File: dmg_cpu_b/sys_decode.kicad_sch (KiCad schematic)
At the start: 82 parts, among them T1 IBUF, T2 IBUF

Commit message: CH1 Regs page completed.
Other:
- company: (none) -> CC-BY-SA-4.0 Régis Galland & Michael Singer -- Derived work from Furrtek
- title: (none) -> DMG CPU B
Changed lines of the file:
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@@
 (kicad_sch (version 20211123) (generator eeschema)
   (paper "A3")
+  (title_block
+    (title "DMG CPU B")
+    (date "2022-03-12")
+    (rev "0")
+    (company "CC-BY-SA-4.0 Régis Galland & Michael Singer -- Derived work from Furrtek")
+    (comment 1 "https://github.com/msinger/dmg-schematics")
+  )
   (junction (at 48.895 224.79) (diameter 0) (color 0 0 0 0)
   )

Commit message: First lot of fixes based on issues found.
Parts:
- added ADYR, AFOP: INVERTER_B, symbol DMG_CPU_Cells:INVERTER_B
- added AJEC, AKAJ, ANOC, ARAR, ASUZ, ATAJ, BEDA, BENU: TRI_INV_IF0, symbol DMG_CPU_Cells:TRI_INV_IF0
- added APYS: NOR_2, symbol DMG_CPU_Cells:NOR_2
- added AXYN: INVERTER_A, symbol DMG_CPU_Cells:INVERTER_A
- renumbered RESET to ~{RESET}
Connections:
- net BEDO: now also AXYN.1
- net D0: now also ANOC.3
- net D1: now also ATAJ.3
- net D2: now also AJEC.3
- net D3: now also ASUZ.3
- net D4: now also BENU.3
- net D5: now also AKAJ.3
- net D6: now also ARAR.3
- net D7: now also BEDA.3
- net GND: now also AJEC.2, AKAJ.2, ANOC.2, ARAR.2, ASUZ.2, ATAJ.2, BEDA.2, BENU.2
- net T1~{T2}: now also APYS.1
- new net: AFOP.2, AJEC.1 (~{ENA}), AKAJ.1 (~{ENA}), ANOC.1 (~{ENA}), ARAR.1 (~{ENA}), ASUZ.1 (~{ENA}), ATAJ.1 (~{ENA}), BEDA.1 (~{ENA}), BENU.1 (~{ENA})
- new net: ADYR.2, APYS.2
- new net: AFOP.1, APYS.3
- new net: ADYR.1, AXYN.2
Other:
- note removed: "This part is activated in test mode."
- moved on the sheet: AMUT, APER, APET, BAKO, BURO, LECO, LEXY, RARU, RASE, REJY, REKA, ROMY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

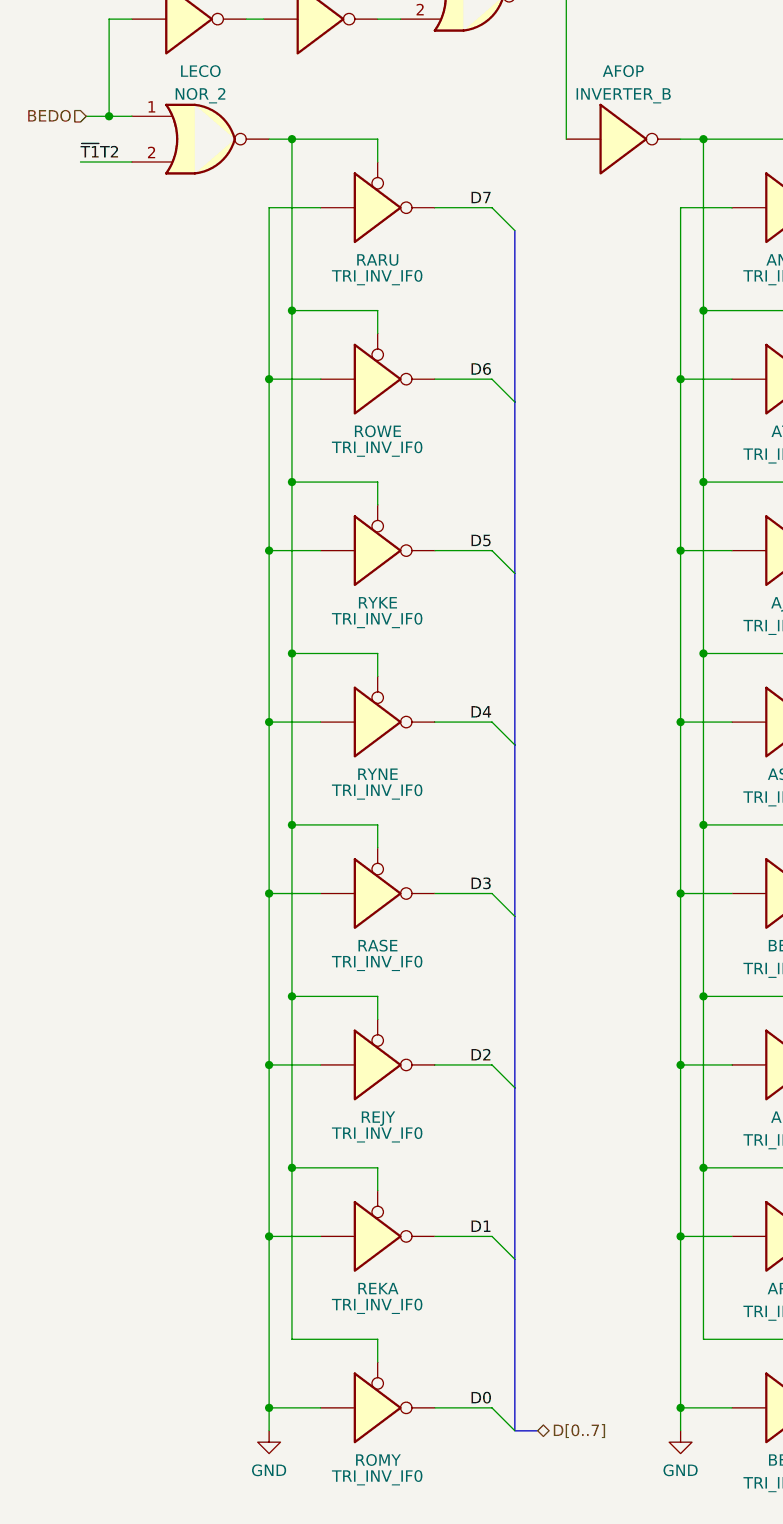
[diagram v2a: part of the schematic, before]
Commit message: CH1 SWEEP page added.
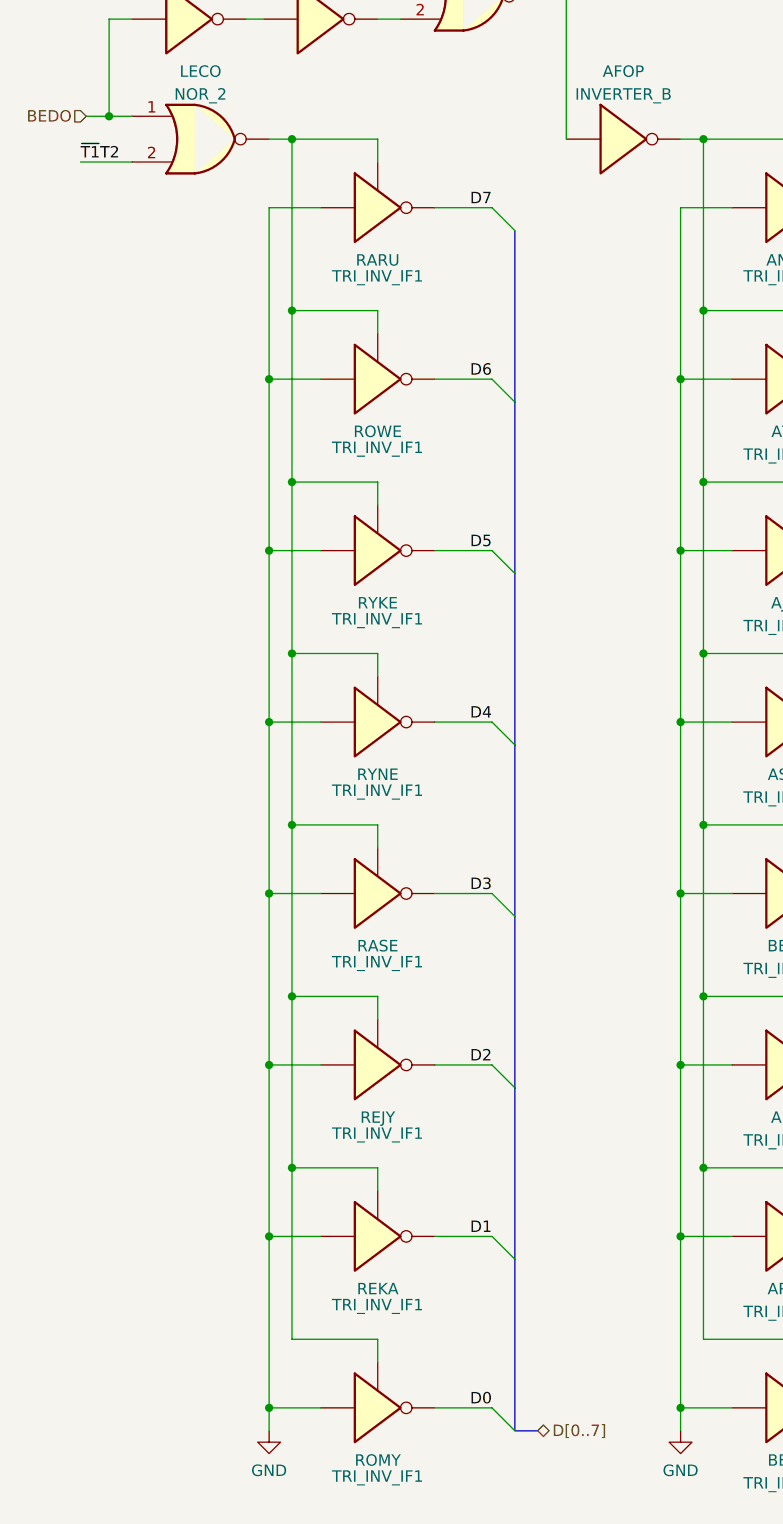
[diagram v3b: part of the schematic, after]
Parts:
- RARU, RASE, REJY, REKA, ROMY, ROWE, RYKE, RYNE: value TRI_INV_IF0 -> TRI_INV_IF1; symbol DMG_CPU_Cells:TRI_INV_IF0 -> DMG_CPU_Cells:TRI_INV_IF1
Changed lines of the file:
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@@
     (pin "2")
   )
-  (symbol (lib_name "TRI_INV_IF0_7") (lib_id "DMG_CPU_Cells:TRI_INV_IF0") (at 56.515 247.65 0) (unit 1)
+  (symbol (lib_id "DMG_CPU_Cells:TRI_INV_IF1") (at 56.515 247.65 0) (unit 1)
     (in_bom yes) (on_board yes) (fields_autoplaced)
     (property "Reference" "REKA" (id 0) (at 56.515 253.4904 0))
-    (property "Value" "TRI_INV_IF0" (id 1) (at 56.515 255.27 0))
+    (property "Value" "TRI_INV_IF1" (id 1) (at 56.515 255.27 0))
     (property "Footprint" "" (id 2) (at 53.975 247.65 0)
       (effects (font (size 1.27 1.27)) hide)
     )
-    (property "Datasheet" "http://iceboy.a-singer.de/doc/dmg_cells.html#tri_inv_if0" (id 3) (at 57.785 257.81 0)
+    (property "Datasheet" "http://iceboy.a-singer.de/doc/dmg_cells.html#tri_inv_if1" (id 3) (at 57.785 257.81 0)
       (effects (font (size 1.27 1.27)) hide)
     )
@@
     (pin "2")
   )
-  (symbol (lib_name "TRI_INV_IF0_3") (lib_id "DMG_CPU_Cells:TRI_INV_IF0") (at 56.515 171.45 0) (unit 1)
+  (symbol (lib_id "DMG_CPU_Cells:TRI_INV_IF1") (at 56.515 171.45 0) (unit 1)
     (in_bom yes) (on_board yes) (fields_autoplaced)
     (property "Reference" "RYKE" (id 0) (at 56.515 177.2904 0))
-    (property "Value" "TRI_INV_IF0" (id 1) (at 56.515 179.07 0))
+    (property "Value" "TRI_INV_IF1" (id 1) (at 56.515 179.07 0))
     (property "Footprint" "" (id 2) (at 53.975 171.45 0)
       (effects (font (size 1.27 1.27)) hide)
     )
-    (property "Datasheet" "http://iceboy.a-singer.de/doc/dmg_cells.html#tri_inv_if0" (id 3) (at 57.785 181.61 0)
-      (effects (font (size 1.27 1.27)) hide)
-    )
-    (pin "2")
-    (pin "3")
-    (pin "1")
-  )
-  (symbol (lib_name "TRI_INV_IF0_5") (lib_id "DMG_CPU_Cells:TRI_INV_IF0") (at 56.515 266.7 0) (unit 1)
+    (property "Datasheet" "http://iceboy.a-singer.de/doc/dmg_cells.html#tri_inv_if1" (id 3) (at 57.785 181.61 0)
+      (effects (font (size 1.27 1.27)) hide)
+    )
+    (pin "2")
+    (pin "3")
+    (pin "1")
+  )
+  (symbol (lib_id "DMG_CPU_Cells:TRI_INV_IF1") (at 56.515 266.7 0) (unit 1)
     (in_bom yes) (on_board yes) (fields_autoplaced)
     (property "Reference" "ROMY" (id 0) (at 56.515 272.5404 0))
-    (property "Value" "TRI_INV_IF0" (id 1) (at 56.515 274.32 0))
+    (property "Value" "TRI_INV_IF1" (id 1) (at 56.515 274.32 0))
     (property "Footprint" "" (id 2) (at 53.975 266.7 0)
       (effects (font (size 1.27 1.27)) hide)
     )
-    (property "Datasheet" "http://iceboy.a-singer.de/doc/dmg_cells.html#tri_inv_if0" (id 3) (at 57.785 276.86 0)
+    (property "Datasheet" "http://iceboy.a-singer.de/doc/dmg_cells.html#tri_inv_if1" (id 3) (at 57.785 276.86 0)
       (effects (font (size 1.27 1.27)) hide)
     )
@@
     (pin "2")
   )
-  (symbol (lib_name "TRI_INV_IF0_6") (lib_id "DMG_CPU_Cells:TRI_INV_IF0") (at 56.515 228.6 0) (unit 1)
+  (symbol (lib_id "DMG_CPU_Cells:TRI_INV_IF1") (at 56.515 228.6 0) (unit 1)
     (in_bom yes) (on_board yes) (fields_autoplaced)
     (property "Reference" "REJY" (id 0) (at 56.515 234.4404 0))
-    (property "Value" "TRI_INV_IF0" (id 1) (at 56.515 236.22 0))
+    (property "Value" "TRI_INV_IF1" (id 1) (at 56.515 236.22 0))
     (property "Footprint" "" (id 2) (at 53.975 228.6 0)
       (effects (font (size 1.27 1.27)) hide)
     )
-    (property "Datasheet" "http://iceboy.a-singer.de/doc/dmg_cells.html#tri_inv_if0" (id 3) (at 57.785 238.76 0)
-      (effects (font (size 1.27 1.27)) hide)
-    )
-    (pin "2")
-    (pin "3")
-    (pin "1")
-  )
-  (symbol (lib_name "TRI_INV_IF0_4") (lib_id "DMG_CPU_Cells:TRI_INV_IF0") (at 56.515 190.5 0) (unit 1)
+    (property "Datasheet" "http://iceboy.a-singer.de/doc/dmg_cells.html#tri_inv_if1" (id 3) (at 57.785 238.76 0)
+      (effects (font (size 1.27 1.27)) hide)
+    )
+    (pin "2")
+    (pin "3")
+    (pin "1")
+  )
+  (symbol (lib_id "DMG_CPU_Cells:TRI_INV_IF1") (at 56.515 190.5 0) (unit 1)
     (in_bom yes) (on_board yes) (fields_autoplaced)
     (property "Reference" "RYNE" (id 0) (at 56.515 196.3404 0))
-    (property "Value" "TRI_INV_IF0" (id 1) (at 56.515 198.12 0))
+    (property "Value" "TRI_INV_IF1" (id 1) (at 56.515 198.12 0))
     (property "Footprint" "" (id 2) (at 53.975 190.5 0)
       (effects (font (size 1.27 1.27)) hide)
     )
-    (property "Datasheet" "http://iceboy.a-singer.de/doc/dmg_cells.html#tri_inv_if0" (id 3) (at 57.785 200.66 0)
+    (property "Datasheet" "http://iceboy.a-singer.de/doc/dmg_cells.html#tri_inv_if1" (id 3) (at 57.785 200.66 0)
       (effects (font (size 1.27 1.27)) hide)
     )
@@
     (pin "3")
   )
-  (symbol (lib_name "TRI_INV_IF0_1") (lib_id "DMG_CPU_Cells:TRI_INV_IF0") (at 56.515 152.4 0) (unit 1)
+  (symbol (lib_id "DMG_CPU_Cells:TRI_INV_IF1") (at 56.515 152.4 0) (unit 1)
     (in_bom yes) (on_board yes) (fields_autoplaced)
     (property "Reference" "ROWE" (id 0) (at 56.515 158.2404 0))
-    (property "Value" "TRI_INV_IF0" (id 1) (at 56.515 160.02 0))
+    (property "Value" "TRI_INV_IF1" (id 1) (at 56.515 160.02 0))
     (property "Footprint" "" (id 2) (at 53.975 152.4 0)
       (effects (font (size 1.27 1.27)) hide)
     )
-    (property "Datasheet" "http://iceboy.a-singer.de/doc/dmg_cells.html#tri_inv_if0" (id 3) (at 57.785 162.56 0)
+    (property "Datasheet" "http://iceboy.a-singer.de/doc/dmg_cells.html#tri_inv_if1" (id 3) (at 57.785 162.56 0)
       (effects (font (size 1.27 1.27)) hide)
     )
@@
     (pin "4")
   )
-  (symbol (lib_name "TRI_INV_IF0_2") (lib_id "DMG_CPU_Cells:TRI_INV_IF0") (at 56.515 133.35 0) (unit 1)
+  (symbol (lib_id "DMG_CPU_Cells:TRI_INV_IF1") (at 56.515 133.35 0) (unit 1)
     (in_bom yes) (on_board yes) (fields_autoplaced)
     (property "Reference" "RARU" (id 0) (at 56.515 139.1904 0))
-    (property "Value" "TRI_INV_IF0" (id 1) (at 56.515 140.97 0))
+    (property "Value" "TRI_INV_IF1" (id 1) (at 56.515 140.97 0))
     (property "Footprint" "" (id 2) (at 53.975 133.35 0)
       (effects (font (size 1.27 1.27)) hide)
     )
-    (property "Datasheet" "http://iceboy.a-singer.de/doc/dmg_cells.html#tri_inv_if0" (id 3) (at 57.785 143.51 0)
+    (property "Datasheet" "http://iceboy.a-singer.de/doc/dmg_cells.html#tri_inv_if1" (id 3) (at 57.785 143.51 0)
       (effects (font (size 1.27 1.27)) hide)
     )
@@
     (pin "1")
   )
-  (symbol (lib_id "DMG_CPU_Cells:TRI_INV_IF0") (at 56.515 209.55 0) (unit 1)
+  (symbol (lib_id "DMG_CPU_Cells:TRI_INV_IF1") (at 56.515 209.55 0) (unit 1)
     (in_bom yes) (on_board yes) (fields_autoplaced)
     (property "Reference" "RASE" (id 0) (at 56.515 215.3904 0))
-    (property "Value" "TRI_INV_IF0" (id 1) (at 56.515 217.17 0))
+    (property "Value" "TRI_INV_IF1" (id 1) (at 56.515 217.17 0))
     (property "Footprint" "" (id 2) (at 53.975 209.55 0)
       (effects (font (size 1.27 1.27)) hide)
     )
-    (property "Datasheet" "http://iceboy.a-singer.de/doc/dmg_cells.html#tri_inv_if0" (id 3) (at 57.785 219.71 0)
-      (effects (font (size 1.27 1.27)) hide)
-    )
+    (property "Datasheet" "http://iceboy.a-singer.de/doc/dmg_cells.html#tri_inv_if1" (id 3) (at 57.785 219.71 0)
+      (effects (font (size 1.27 1.27)) hide)
+    )

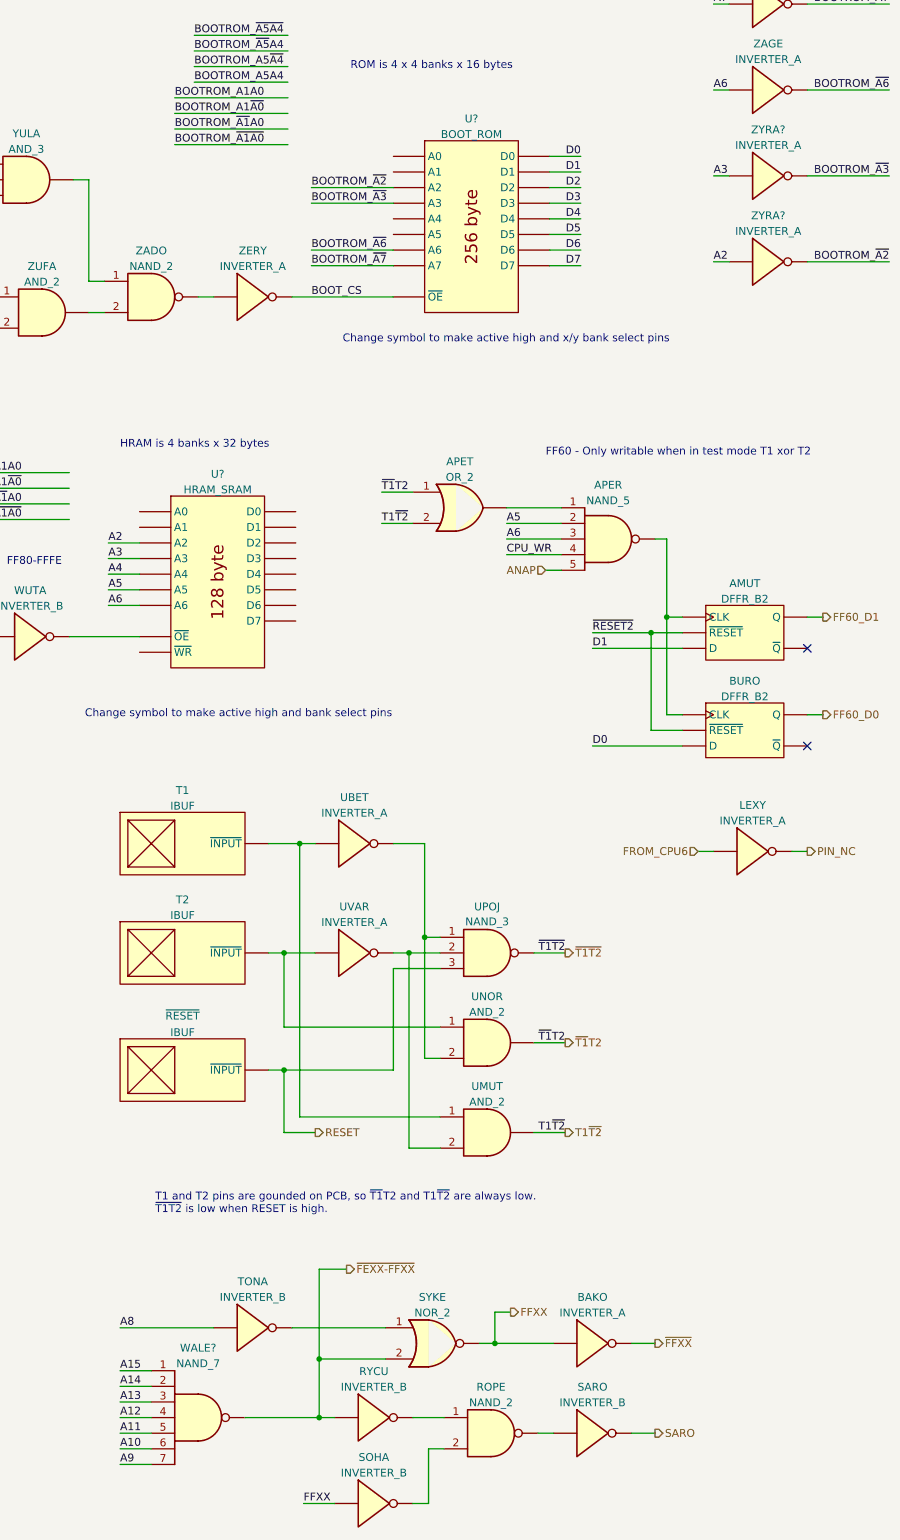
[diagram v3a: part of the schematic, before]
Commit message: fixes made following review
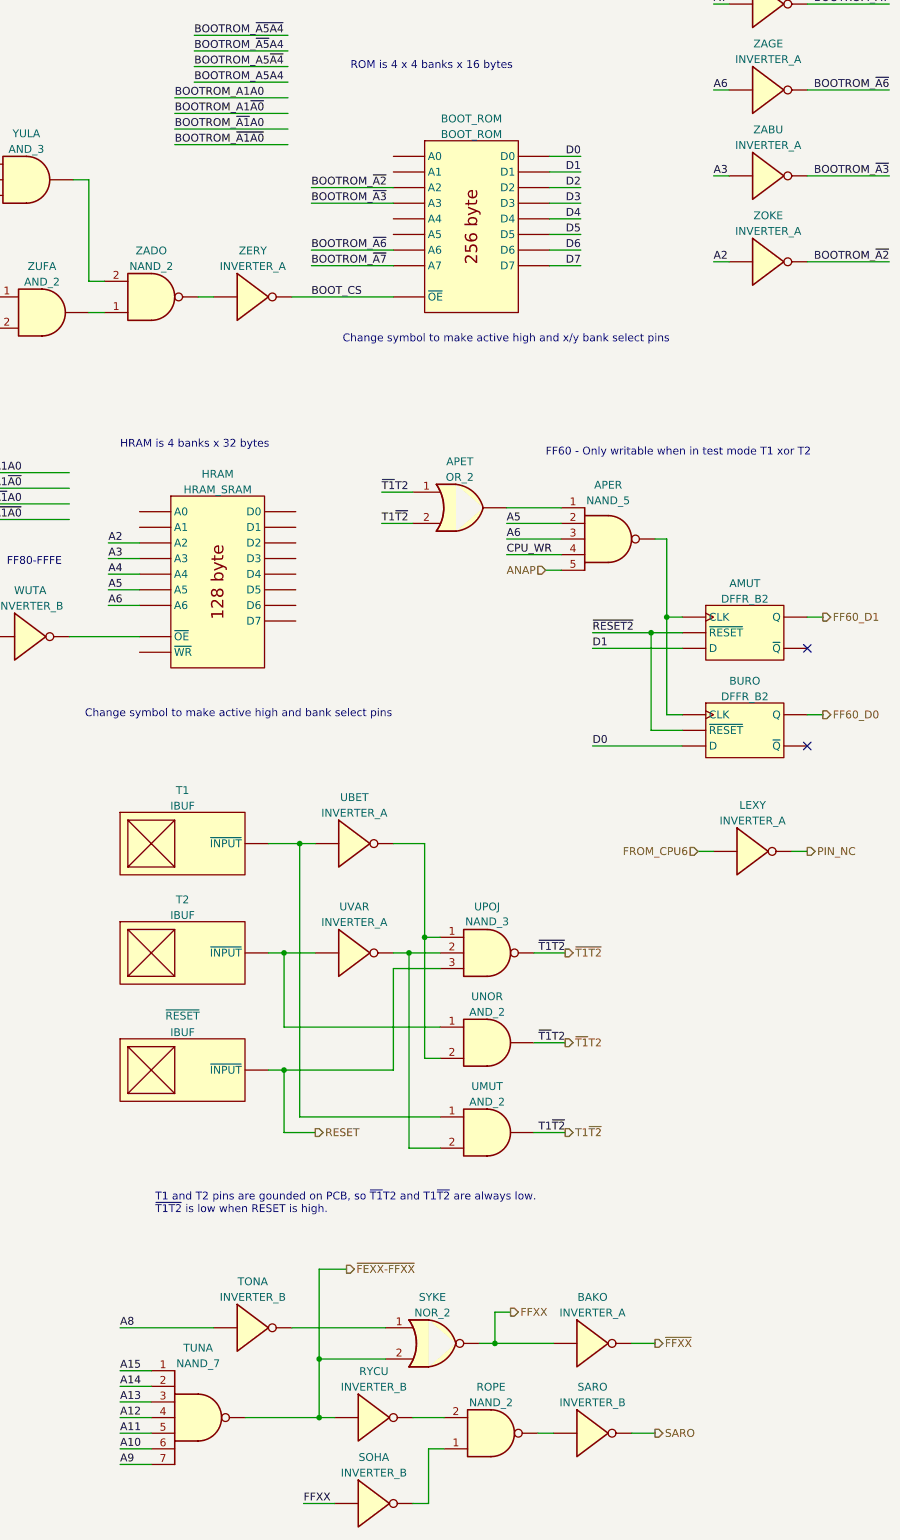
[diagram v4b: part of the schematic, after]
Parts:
- gave numbers to parts that had none: 5
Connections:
- net at ROPE.1: now also SOHA.2; no longer RYCU.2
- net at ROPE.2: now also RYCU.2; no longer SOHA.2
- net at ZADO.1: now also ZUFA.3; no longer YULA.4
- net at ZADO.2: now also YULA.4; no longer ZUFA.3
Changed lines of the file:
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@@
     (pin "2")
   )
-  (symbol (lib_id "DMG_CPU_Cells:NAND_2") (at 254.635 262.255 0) (unit 1)
+  (symbol (lib_id "DMG_CPU_Cells:NAND_2") (at 254.635 262.255 0) (mirror x) (unit 1)
     (in_bom yes) (on_board yes) (fields_autoplaced)
     (property "Reference" "ROPE" (id 0) (at 254.635 254.7452 0))
@@
       (effects (font (size 1.27 1.27)) hide)
     )
-    (property "Datasheet" "http://iceboy.a-singer.de/doc/dmg_cells.html#nand2" (id 3) (at 254.635 269.875 0)
+    (property "Datasheet" "http://iceboy.a-singer.de/doc/dmg_cells.html#nand2" (id 3) (at 254.635 254.635 0)
       (effects (font (size 1.27 1.27)) hide)
     )
@@
   (symbol (lib_id "DMG_CPU_Cells:INVERTER_A") (at 299.72 57.785 0) (unit 1)
     (in_bom yes) (on_board yes) (fields_autoplaced)
-    (property "Reference" "ZYRA?" (id 0) (at 299.72 50.2752 0))
+    (property "Reference" "ZABU" (id 0) (at 299.72 50.2752 0))
     (property "Value" "INVERTER_A" (id 1) (at 299.72 52.8121 0))
     (property "Footprint" "" (id 2) (at 297.18 57.785 0)
@@
   (symbol (lib_id "DMG_CPU_Cells:NAND_7") (at 207.01 259.715 0) (unit 1)
     (in_bom yes) (on_board yes) (fields_autoplaced)
-    (property "Reference" "WALE?" (id 0) (at 207.01 248.3952 0))
+    (property "Reference" "TUNA" (id 0) (at 207.01 248.3952 0))
     (property "Value" "NAND_7" (id 1) (at 207.01 250.9321 0))
     (property "Footprint" "" (id 2) (at 207.01 259.715 0)
@@
     (pin "3")
   )
-  (symbol (lib_id "DMG_CPU_Cells:NAND_2") (at 199.39 77.47 0) (unit 1)
+  (symbol (lib_id "DMG_CPU_Cells:NAND_2") (at 199.39 77.47 0) (mirror x) (unit 1)
     (in_bom yes) (on_board yes) (fields_autoplaced)
     (property "Reference" "ZADO" (id 0) (at 199.39 69.9602 0))
@@
       (effects (font (size 1.27 1.27)) hide)
     )
-    (property "Datasheet" "http://iceboy.a-singer.de/doc/dmg_cells.html#nand2" (id 3) (at 199.39 85.09 0)
+    (property "Datasheet" "http://iceboy.a-singer.de/doc/dmg_cells.html#nand2" (id 3) (at 199.39 69.85 0)
       (effects (font (size 1.27 1.27)) hide)
     )
@@
   (symbol (lib_id "DMG_CPU_Cells:BOOT_ROM") (at 251.46 66.04 0) (unit 1)
     (in_bom yes) (on_board yes) (fields_autoplaced)
-    (property "Reference" "U?" (id 0) (at 251.46 48.4972 0))
+    (property "Reference" "BOOT_ROM" (id 0) (at 251.46 48.4972 0))
     (property "Value" "BOOT_ROM" (id 1) (at 251.46 51.0341 0))
     (property "Footprint" "" (id 2) (at 251.46 66.04 0)
@@
   (symbol (lib_id "DMG_CPU_Cells:INVERTER_A") (at 299.72 71.755 0) (unit 1)
     (in_bom yes) (on_board yes) (fields_autoplaced)
-    (property "Reference" "ZYRA?" (id 0) (at 299.72 64.2452 0))
+    (property "Reference" "ZOKE" (id 0) (at 299.72 64.2452 0))
     (property "Value" "INVERTER_A" (id 1) (at 299.72 66.7821 0))
     (property "Footprint" "" (id 2) (at 297.18 71.755 0)
@@
   (symbol (lib_id "DMG_CPU_Cells:HRAM_SRAM") (at 210.185 123.825 0) (unit 1)
     (in_bom yes) (on_board yes) (fields_autoplaced)
-    (property "Reference" "U?" (id 0) (at 210.185 106.2822 0))
+    (property "Reference" "HRAM" (id 0) (at 210.185 106.2822 0))
     (property "Value" "HRAM_SRAM" (id 1) (at 210.185 108.8191 0))
     (property "Footprint" "" (id 2) (at 210.185 123.825 0)
